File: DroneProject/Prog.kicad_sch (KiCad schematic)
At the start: 17 parts, among them SW131 L101011MS02Q, U131 NC7SZ04P5X, U132 TS3A4751PWR, U133 SN74LVC1G08DBVR, U134 TS3A4751PWR, U135 SN74LVC1G08DBVR, U136 TS3A4751PWR

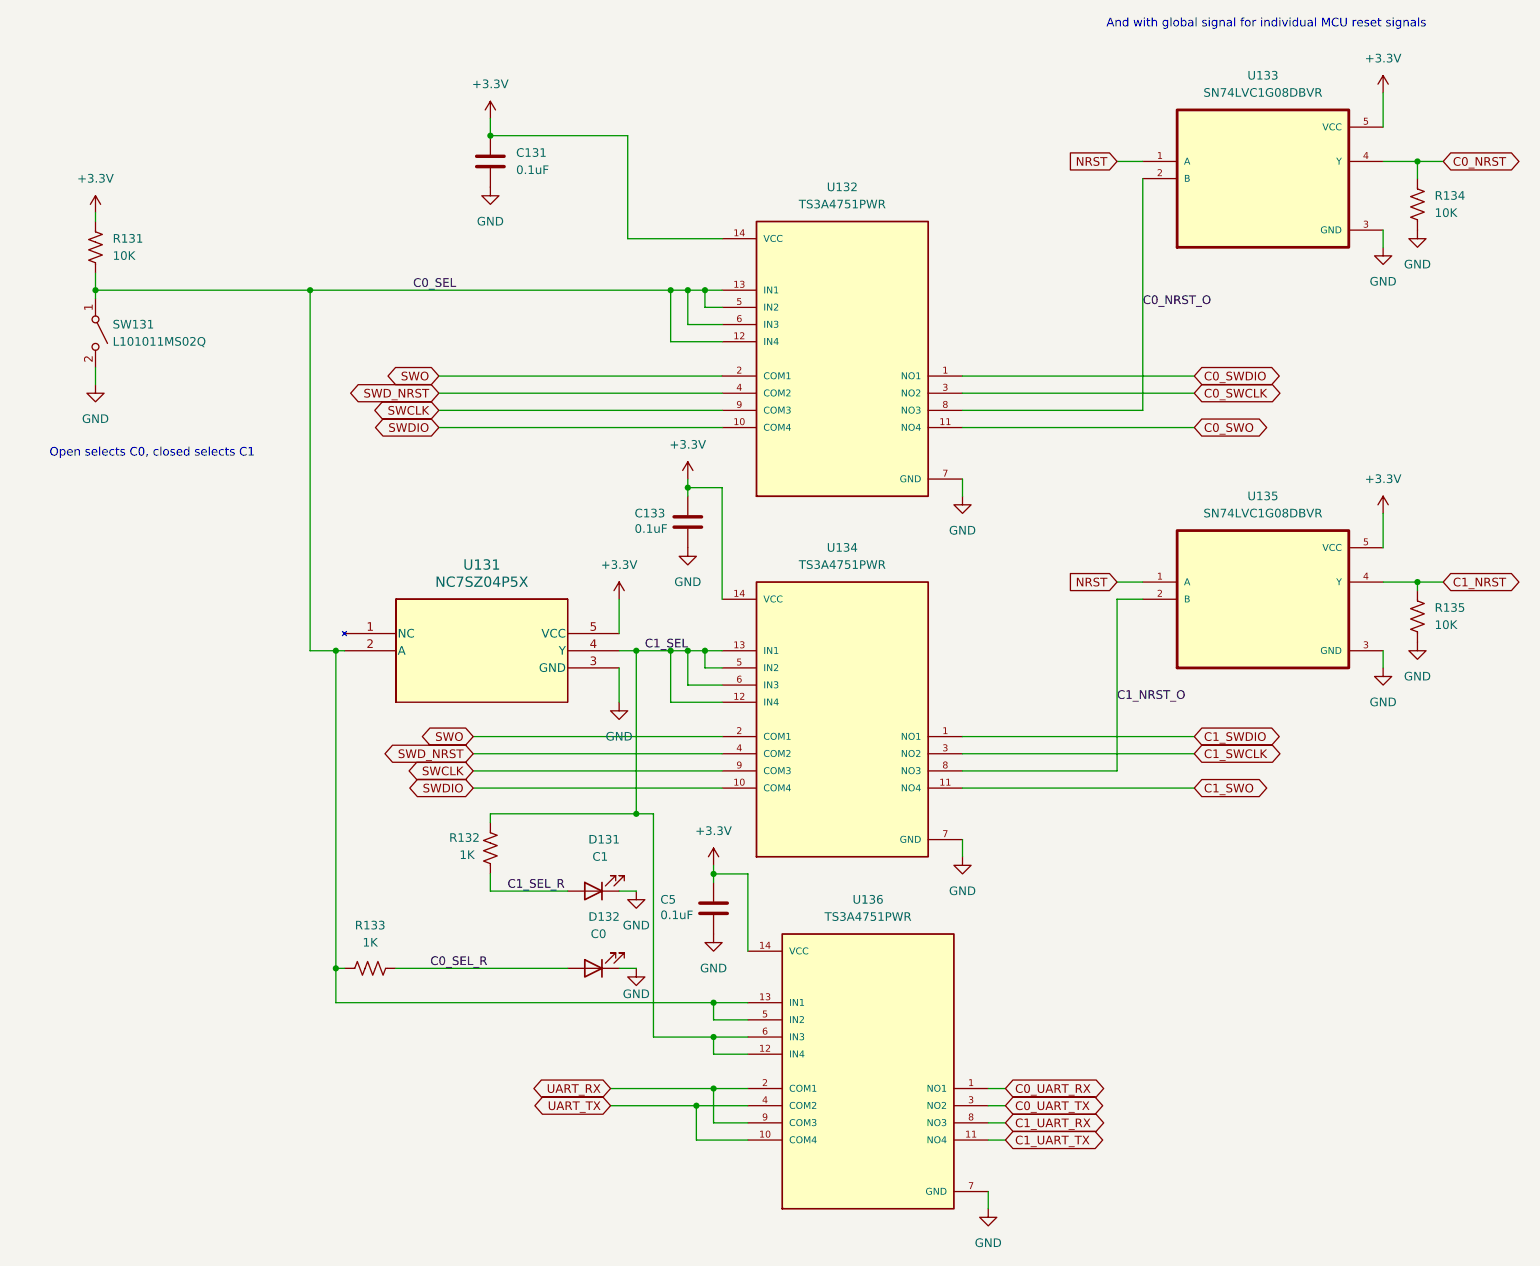
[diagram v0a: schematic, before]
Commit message: Changed motor controller to higher pin count MCU.  Defined all the pins for 3x PWM control over 4 motors.  Renamed a couple of global IO signals to indicate MCU origin (C0 vs C1)
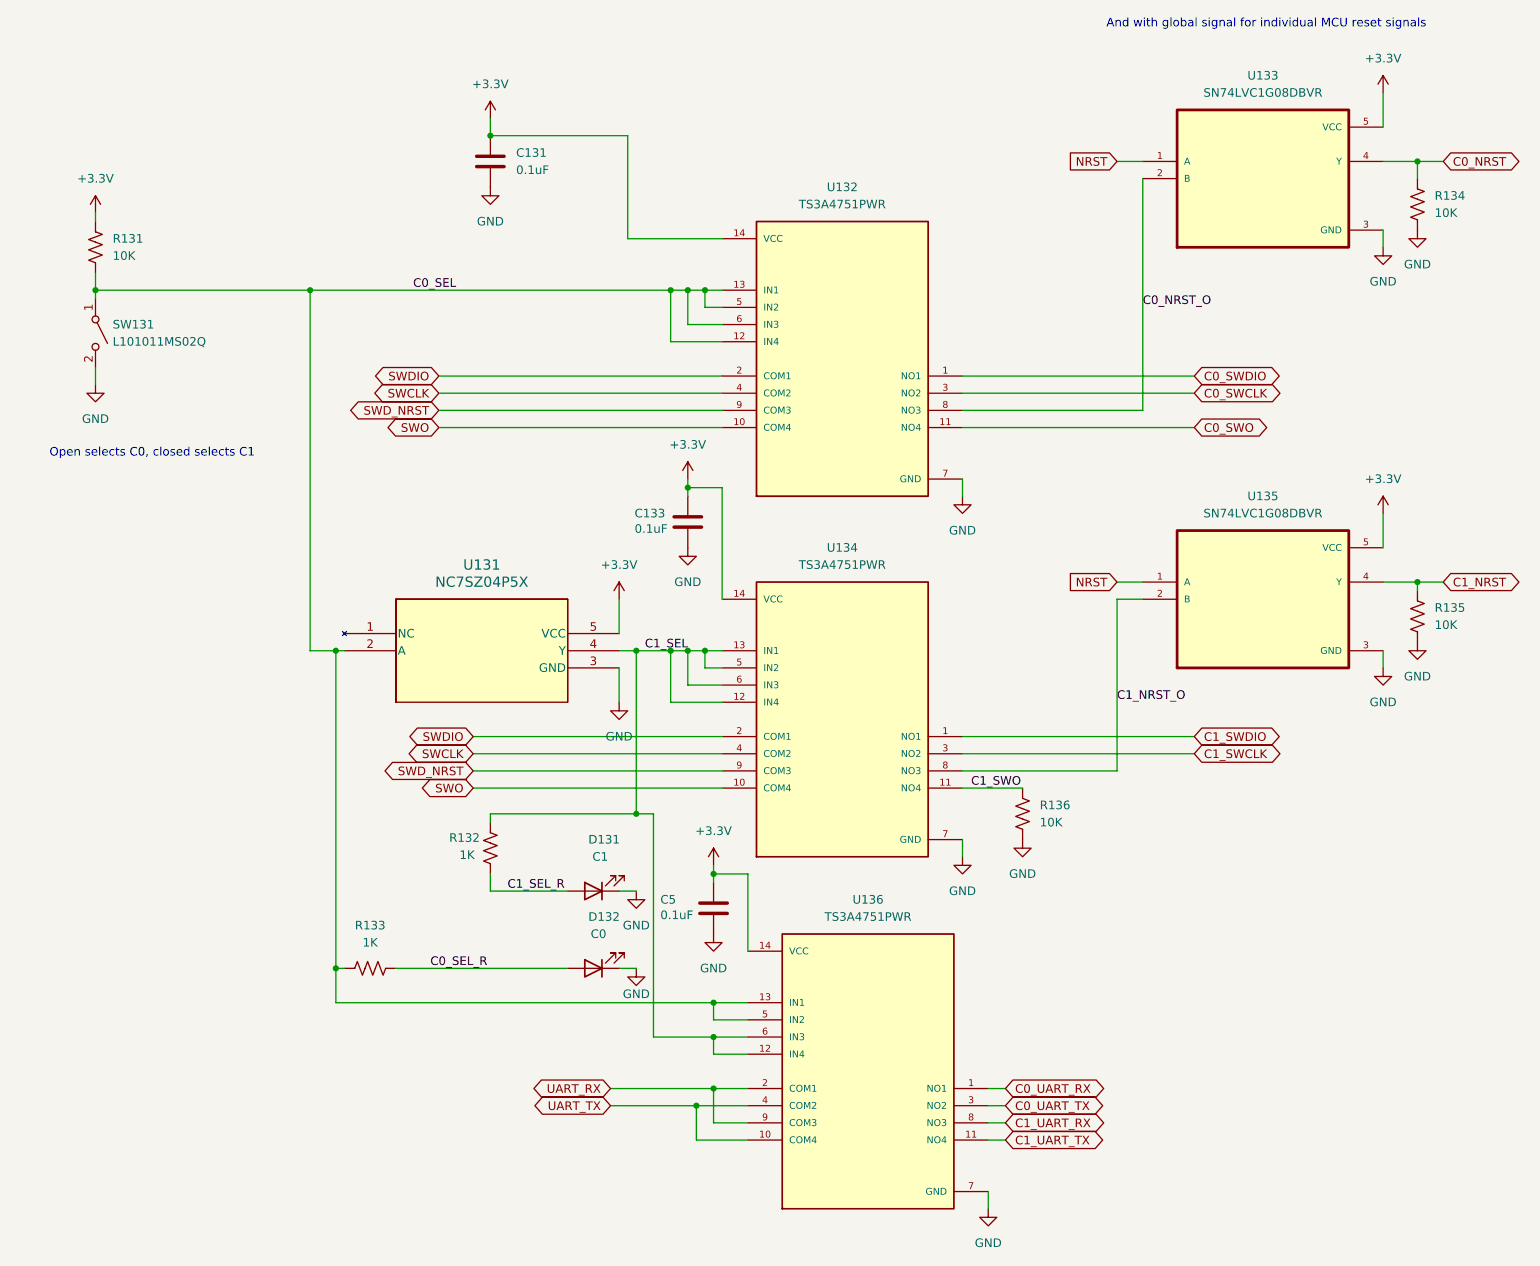
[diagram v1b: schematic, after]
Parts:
- added R136: 10K, Resistor_SMD:R_0402_1005Metric, symbol Device:R_US
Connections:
- net C1_SWO: now also R136.2
- net GND: now also R136.1
- net SWCLK: now also U132.4 (COM2), U134.4 (COM2); no longer U132.9 (COM3), U134.9 (COM3)
- net SWDIO: now also U132.2 (COM1), U134.2 (COM1); no longer U132.10 (COM4), U134.10 (COM4)
- net SWD_NRST: now also U132.9 (COM3), U134.9 (COM3); no longer U132.4 (COM2), U134.4 (COM2)
- net SWO: now also U132.10 (COM4), U134.10 (COM4); no longer U132.2 (COM1), U134.2 (COM1)

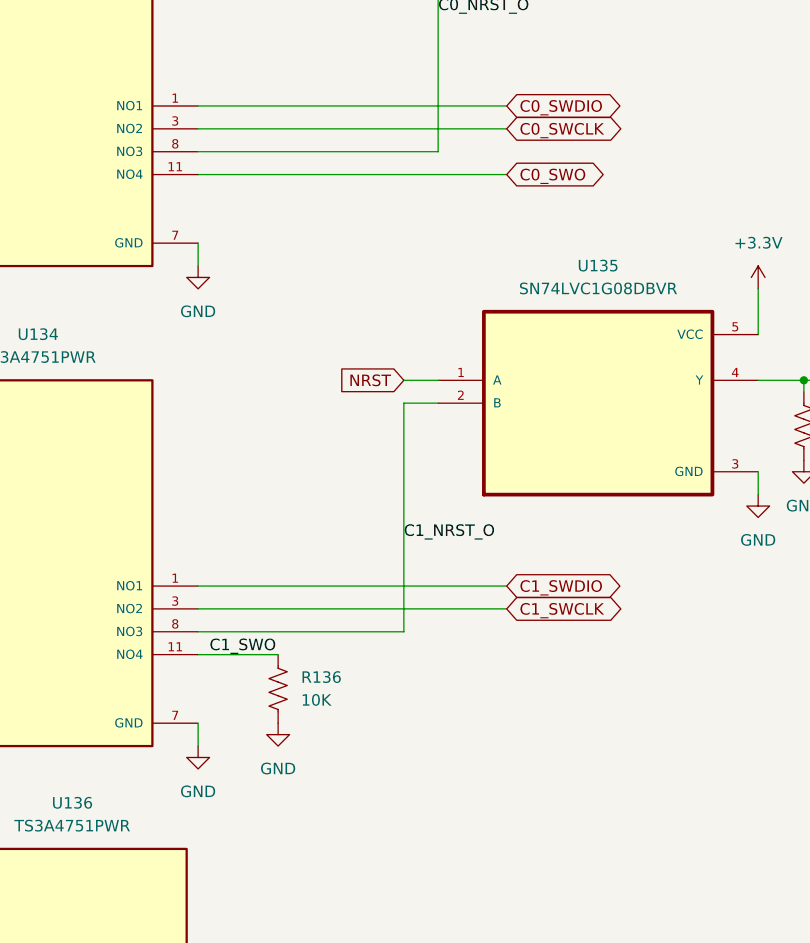
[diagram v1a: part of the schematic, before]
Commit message: Finished motor and C1 designs, still need to rename components on MTR2, 3, and 4 pages
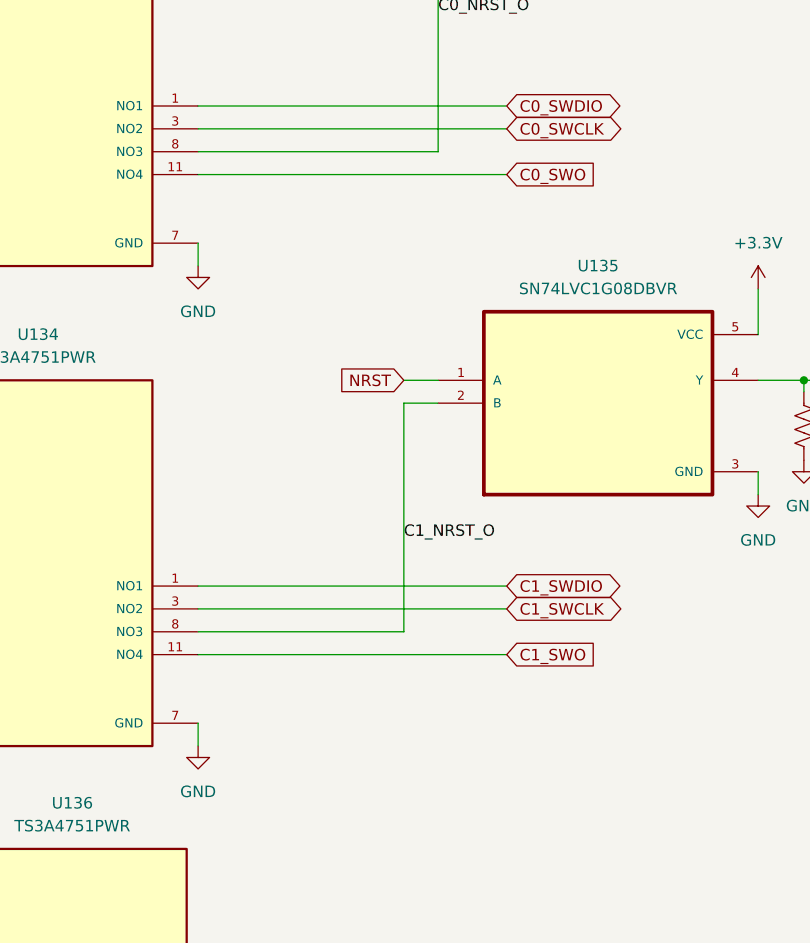
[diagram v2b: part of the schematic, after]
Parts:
- removed R136: 10K, Resistor_SMD:R_0402_1005Metric, symbol Device:R_US
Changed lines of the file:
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@@
 	(wire
 		(pts
-			(xy 153.67 129.54) (xy 162.56 129.54)
+			(xy 153.67 129.54) (xy 187.96 129.54)
 		)
 		(stroke
@@
 	(label "C1_SEL"
 		(at 106.68 109.22 0)
-		(effects
-			(font
-				(size 1.27 1.27)
-			)
-			(justify left bottom)
-		)
-	)
-	(label "C1_SWO"
-		(at 154.94 129.54 0)
 		(effects
 			(font
@@
 		)
 	)
+	(global_label "C1_SWO"
+		(shape input)
+		(at 187.96 129.54 0)
+		(fields_autoplaced yes)
+		(effects
+			(font
+				(size 1.27 1.27)
+			)
+			(justify left)
+		)
+		(property "Intersheetrefs" "${INTERSHEET_REFS}"
+			(at 198.3837 129.54 0)
+			(effects
+				(font
+					(size 1.27 1.27)
+				)
+				(justify left)
+			)
+		)
+	)
 	(global_label "SWDIO"
 		(shape bidirectional)
@@
 	)
 	(global_label "C0_SWO"
-		(shape bidirectional)
+		(shape input)
 		(at 187.96 76.2 0)
 		(fields_autoplaced yes)
@@
 		)
 		(property "Intersheetrefs" "${INTERSHEET_REFS}"
-			(at 199.495 76.2 0)
+			(at 198.3837 76.2 0)
 			(effects
 				(font
@@
 	)
 	(symbol
-		(lib_id "Device:R_US")
-		(at 162.56 133.35 180)
-		(unit 1)
-		(exclude_from_sim no)
-		(in_bom yes)
-		(on_board yes)
-		(dnp no)
-		(fields_autoplaced yes)
-		(property "Reference" "R136"
-			(at 165.1 132.0799 0)
-			(effects
-				(font
-					(size 1.27 1.27)
-				)
-				(justify right)
-			)
-		)
-		(property "Value" "10K"
-			(at 165.1 134.6199 0)
-			(effects
-				(font
-					(size 1.27 1.27)
-				)
-				(justify right)
-			)
-		)
-		(property "Footprint" "Resistor_SMD:R_0402_1005Metric"
-			(at 161.544 133.096 90)
-			(effects
-				(font
-					(size 1.27 1.27)
-				)
-				(hide yes)
-			)
-		)
-		(property "Datasheet" "~"
-			(at 162.56 133.35 0)
-			(effects
-				(font
-					(size 1.27 1.27)
-				)
-				(hide yes)
-			)
-		)
-		(property "Description" "Resistor, US symbol"
-			(at 162.56 133.35 0)
-			(effects
-				(font
-					(size 1.27 1.27)
-				)
-				(hide yes)
-			)
-		)
-		(pin "1"
-		)
-		(pin "2"
-		)
-		(instances
-			(project "DroneProject"
-				(path "/feb4ca7b-5376-4689-a73b-f56020a5aa30/cacd4093-de6a-46a4-8042-da27bb463aad"
-					(reference "R136")
-					(unit 1)
-				)
-			)
-		)
-	)
-	(symbol
 		(lib_id "power:GND")
 		(at 105.41 156.21 0)
@@
 					(unit 1)
 				)
-			)
-		)
-	)
-	(symbol
-		(lib_id "power:GND")
-		(at 162.56 137.16 0)
-		(unit 1)
-		(exclude_from_sim no)
-		(in_bom yes)
-		(on_board yes)
-		(dnp no)
-		(fields_autoplaced yes)
-		(property "Reference" "#PWR018"
-			(at 162.56 143.51 0)
-			(effects
-				(font
-					(size 1.27 1.27)
-				)
-				(hide yes)
-			)
-		)
-		(property "Value" "GND"
-			(at 162.56 142.24 0)
-			(effects
-				(font
-					(size 1.27 1.27)
-				)
-			)
-		)
-		(property "Footprint" ""
-			(at 162.56 137.16 0)
-			(effects
-				(font
-					(size 1.27 1.27)
-				)
-				(hide yes)
-			)
-		)
-		(property "Datasheet" ""
-			(at 162.56 137.16 0)
-			(effects
-				(font
-					(size 1.27 1.27)
-				)
-				(hide yes)
-			)
-		)
-		(property "Description" "Power symbol creates a global label with name \"GND\" , ground"
-			(at 162.56 137.16 0)
-			(effects
-				(font
-					(size 1.27 1.27)
-				)
-				(hide yes)
-			)
-		)
-		(pin "1"
-		)
-		(instances
-			(project "DroneProject"
-				(path "/feb4ca7b-5376-4689-a73b-f56020a5aa30/cacd4093-de6a-46a4-8042-da27bb463aad"
-					(reference "#PWR018")
-					(unit 1)
-				)

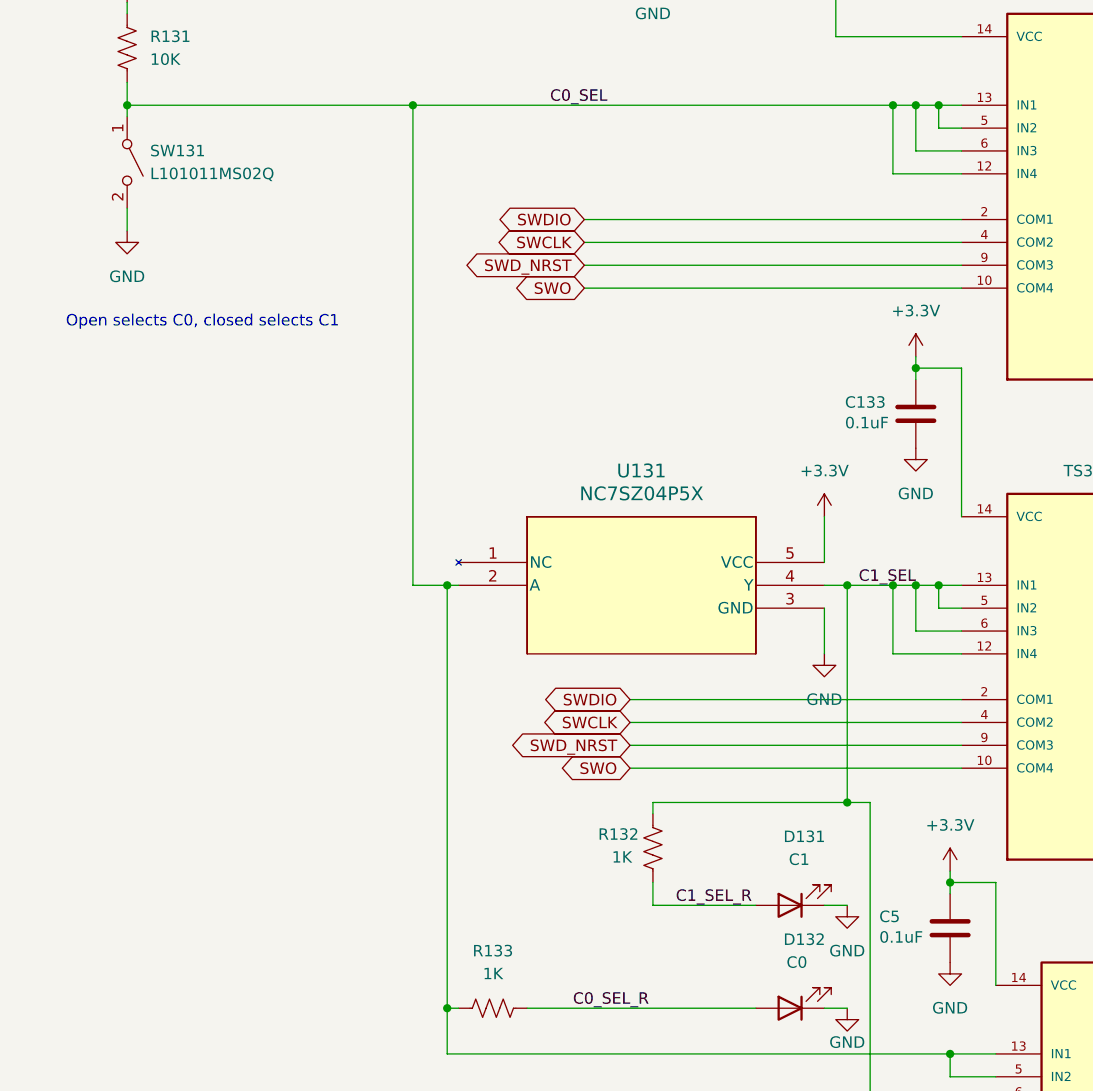
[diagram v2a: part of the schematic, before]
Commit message: Finished most of routing for motor controls, however likely going to revert back and make separate ESC boards for motor control as I think that would honestly be more efficient from both a cost and debug complexity standpoint.
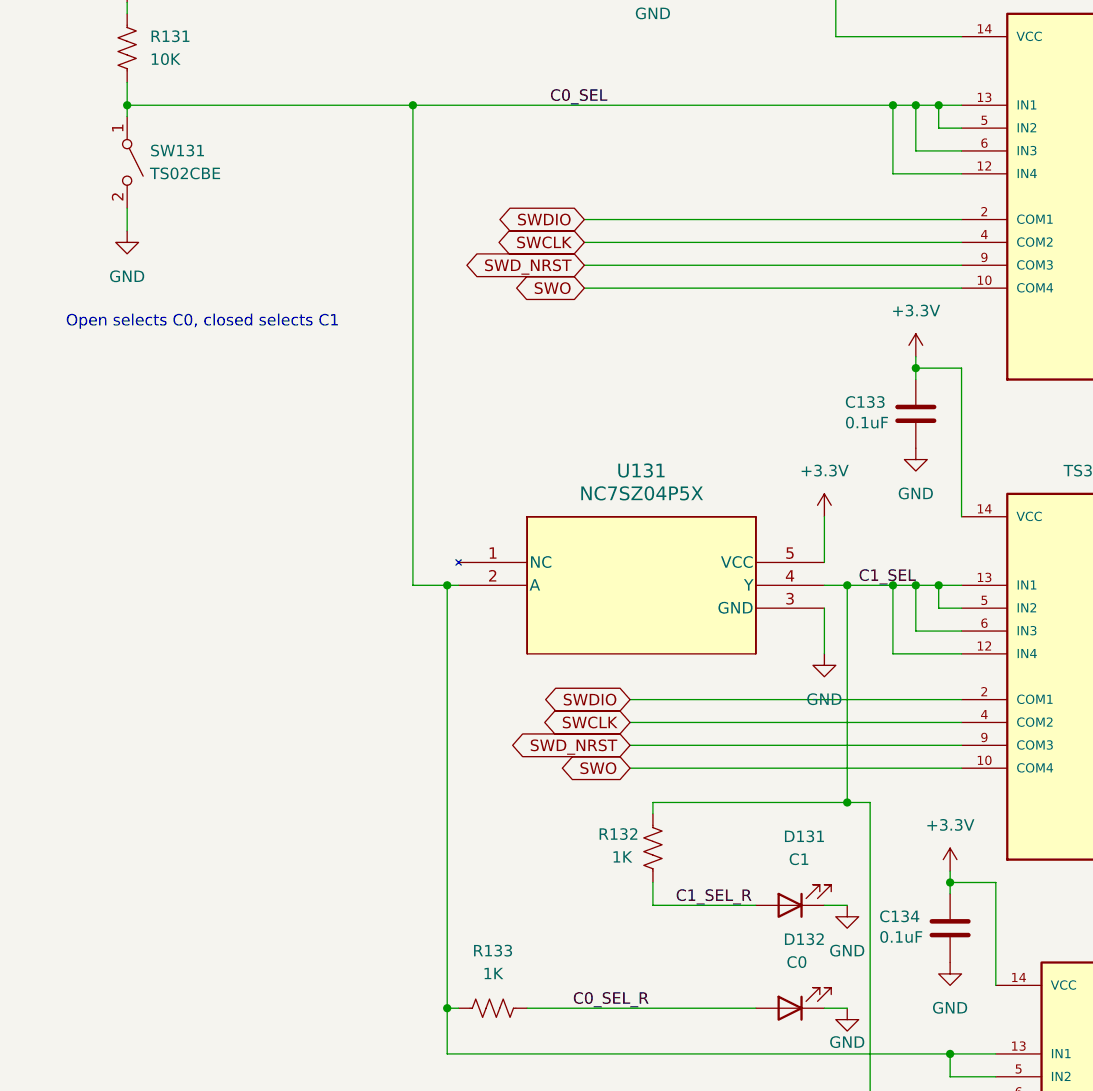
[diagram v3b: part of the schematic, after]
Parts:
- SW131: value L101011MS02Q -> TS02CBE; footprint Library:SW_1MS02Q_CNK -> Library:SW_TS02_10P16X5P08_CNK
- renumbered C5 to C134
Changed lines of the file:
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@@
 			)
 		)
-		(property "Value" "L101011MS02Q"
+		(property "Value" "TS02CBE"
 			(at 27.94 63.4999 90)
 			(effects
@@
 			)
 		)
-		(property "Footprint" "Library:SW_1MS02Q_CNK"
+		(property "Footprint" "Library:SW_TS02_10P16X5P08_CNK"
 			(at 25.4 62.23 0)
 			(effects
@@
 		(on_board yes)
 		(dnp no)
-		(property "Reference" "C5"
+		(property "Reference" "C134"
 			(at 108.966 146.05 0)
 			(effects
@@
 			(project "DroneProject"
 				(path "/feb4ca7b-5376-4689-a73b-f56020a5aa30/cacd4093-de6a-46a4-8042-da27bb463aad"
-					(reference "C5")
-					(unit 1)
-				)
+					(reference "C134")
+					(unit 1)
+				)
